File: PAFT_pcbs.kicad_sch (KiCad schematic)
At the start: 15 parts, among them J1 Conn_01x03, J2 Conn_01x03, J4 Screw_Terminal_01x02, J5 Screw_Terminal_01x02, J6 RPi_GPIO, J8 Screw_Terminal_01x02, J9 Screw_Terminal_01x02

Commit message: Updated schematic
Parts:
- removed J4, J5: Screw_Terminal_01x02, TerminalBlock:TerminalBlock_MaiXu_MX126-5.0-02P_1x02_P5.00mm, symbol Connector:Screw_Terminal_01x02
- added J4: Actuator_L, Connector_PinHeader_2.00mm:PinHeader_1x02_P2.00mm_Vertical, symbol Connector_Generic:Conn_01x02
- added J5: Actuator_R, Connector_PinHeader_2.00mm:PinHeader_1x02_P2.00mm_Vertical, symbol Connector_Generic:Conn_01x02
- J1: value Conn_01x03 -> Servo_R; footprint (none) -> Connector_PinHeader_2.00mm:PinHeader_1x03_P2.00mm_Vertical
- J2: value Conn_01x03 -> Servo_L; footprint (none) -> Connector_PinHeader_2.00mm:PinHeader_1x03_P2.00mm_Vertical
- J8: value Screw_Terminal_01x02 -> 12V_In
- J9: value Screw_Terminal_01x02 -> RPi_Terminal
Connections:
- net HBridge/AOUT1: now also J4.1 (Pin_1)
- net HBridge/AOUT2: now also J4.2 (Pin_2)
- net HBridge/BOUT1: now also J5.1 (Pin_1)
- net HBridge/BOUT2: now also J5.2 (Pin_2)
- net HBridge/FAULT_N: now also J6.35 (BCM19_MISO_PCM_FS)
- net HBridge/SLEEP_N: now also J6.37 (BCM26)
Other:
- removed sheet RPiUSBC
- moved on the sheet: J8, J9, TP1, TP2

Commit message: Added footprints
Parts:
- J6: footprint (none) -> RPi_HAT:RPI_Hat_B+
- TP1: value TestPoint -> 12V; footprint (none) -> TestPoint:TestPoint_Plated_Hole_D2.0mm
- TP2: value TestPoint -> GND; footprint (none) -> TestPoint:TestPoint_Plated_Hole_D2.0mm
- TP3: value TestPoint -> 6V; footprint (none) -> TestPoint:TestPoint_Plated_Hole_D2.0mm
- TP4: value TestPoint -> 5V; footprint (none) -> TestPoint:TestPoint_Plated_Hole_D2.0mm
- TP5: value TestPoint -> PWM_R; footprint (none) -> TestPoint:TestPoint_Plated_Hole_D2.0mm
- TP6: value TestPoint -> PWM_L; footprint (none) -> TestPoint:TestPoint_Plated_Hole_D2.0mm
- TP7: value TestPoint -> SDA; footprint (none) -> TestPoint:TestPoint_Plated_Hole_D2.0mm
- TP8: value TestPoint -> SCL; footprint (none) -> TestPoint:TestPoint_Plated_Hole_D2.0mm
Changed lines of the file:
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@@
 			)
 		)
-		(property "Value" "TestPoint"
+		(property "Value" "SDA"
 			(at 106.68 39.8779 0)
 			(effects
@@
 			)
 		)
-		(property "Footprint" ""
+		(property "Footprint" "TestPoint:TestPoint_Plated_Hole_D2.0mm"
 			(at 109.22 41.91 0)
 			(effects
@@
 			)
 		)
-		(property "Value" "TestPoint"
-			(at 29.464 35.052 0)
-			(effects
-				(font
-					(size 1.27 1.27)
-				)
-				(justify left)
-			)
-		)
-		(property "Footprint" ""
+		(property "Value" "5V"
+			(at 35.56 34.29 0)
+			(effects
+				(font
+					(size 1.27 1.27)
+				)
+				(justify left)
+			)
+		)
+		(property "Footprint" "TestPoint:TestPoint_Plated_Hole_D2.0mm"
 			(at 45.72 36.83 0)
 			(effects
@@
 			)
 		)
-		(property "Value" "TestPoint"
+		(property "Value" "PWM_L"
 			(at 149.86 51.5619 0)
 			(effects
@@
 			)
 		)
-		(property "Footprint" ""
+		(property "Footprint" "TestPoint:TestPoint_Plated_Hole_D2.0mm"
 			(at 142.24 46.99 0)
 			(effects
@@
 			)
 		)
-		(property "Value" "TestPoint"
+		(property "Value" "GND"
 			(at 78.74 121.4119 0)
 			(effects
@@
 			)
 		)
-		(property "Footprint" ""
+		(property "Footprint" "TestPoint:TestPoint_Plated_Hole_D2.0mm"
 			(at 71.12 116.84 0)
 			(effects
@@
 			)
 		)
-		(property "Value" "TestPoint"
+		(property "Value" "6V"
 			(at 157.48 24.6379 0)
 			(effects
@@
 			)
 		)
-		(property "Footprint" ""
+		(property "Footprint" "TestPoint:TestPoint_Plated_Hole_D2.0mm"
 			(at 160.02 26.67 0)
 			(effects
@@
 			)
 		)
-		(property "Value" "TestPoint"
+		(property "Value" "PWM_R"
 			(at 149.86 36.0679 0)
 			(effects
@@
 			)
 		)
-		(property "Footprint" ""
+		(property "Footprint" "TestPoint:TestPoint_Plated_Hole_D2.0mm"
 			(at 152.4 38.1 0)
 			(effects
@@
 			)
 		)
-		(property "Value" "TestPoint"
+		(property "Value" "12V"
 			(at 78.74 112.2679 0)
 			(effects
@@
 			)
 		)
-		(property "Footprint" ""
+		(property "Footprint" "TestPoint:TestPoint_Plated_Hole_D2.0mm"
 			(at 81.28 114.3 0)
 			(effects
@@
 			)
 		)
-		(property "Value" "TestPoint"
+		(property "Value" "SCL"
 			(at 106.68 49.0219 0)
 			(effects
@@
 			)
 		)
-		(property "Footprint" ""
+		(property "Footprint" "TestPoint:TestPoint_Plated_Hole_D2.0mm"
 			(at 99.06 44.45 0)
 			(effects
@@
 			)
 		)
-		(property "Footprint" ""
+		(property "Footprint" "RPi_HAT:RPI_Hat_B+"
 			(at 93.98 39.37 0)
 			(effects

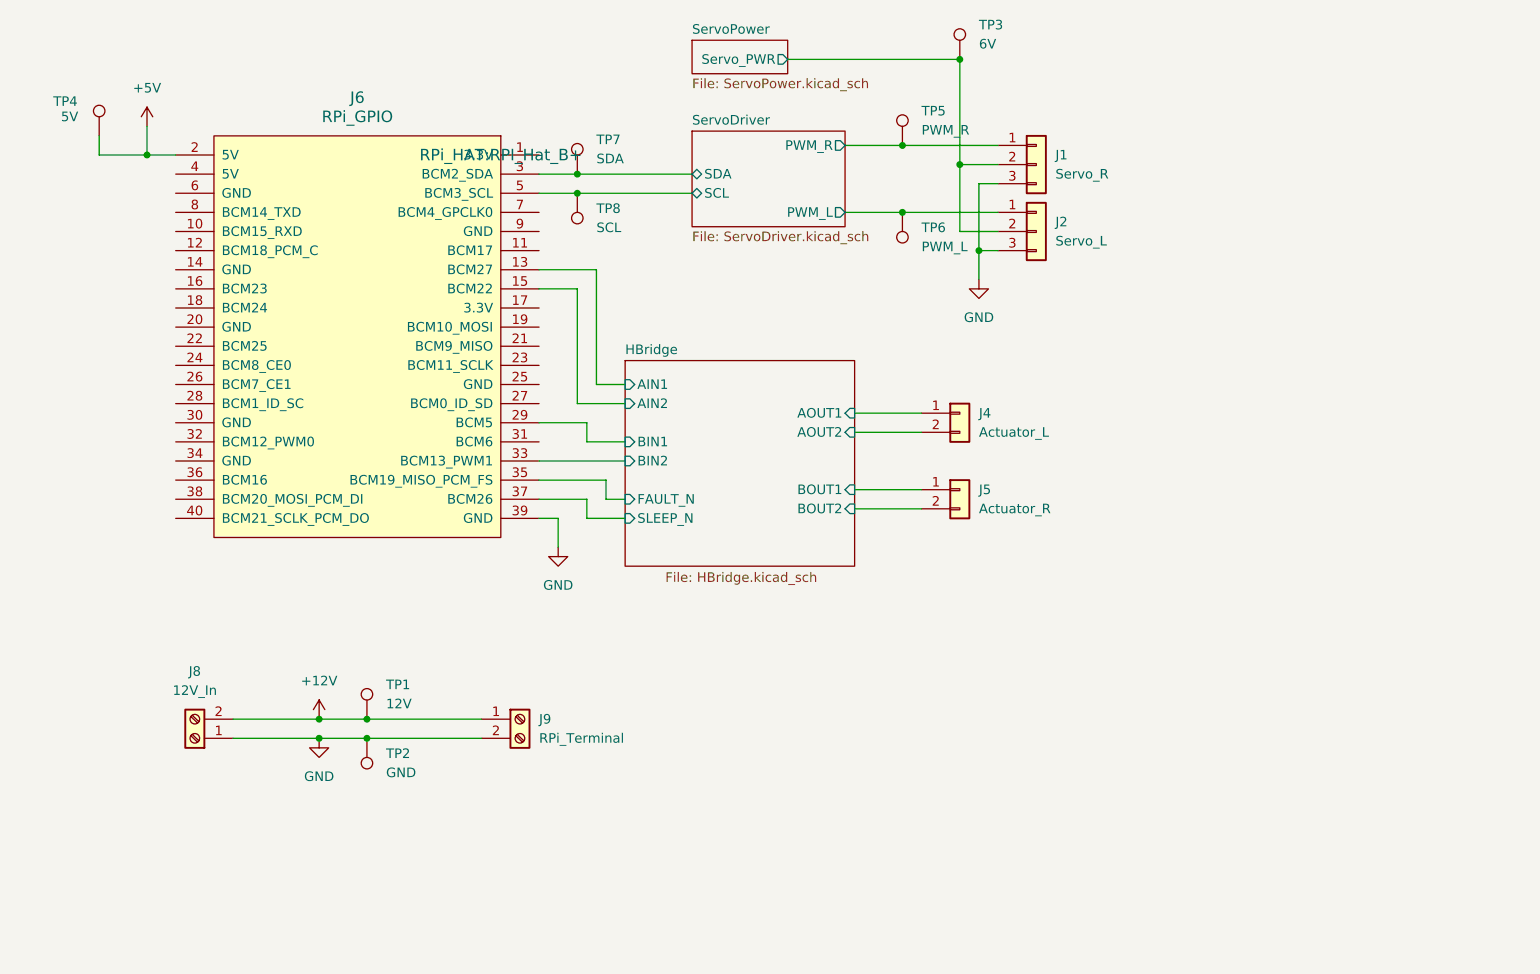
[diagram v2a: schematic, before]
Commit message: PCB Placement and Planes
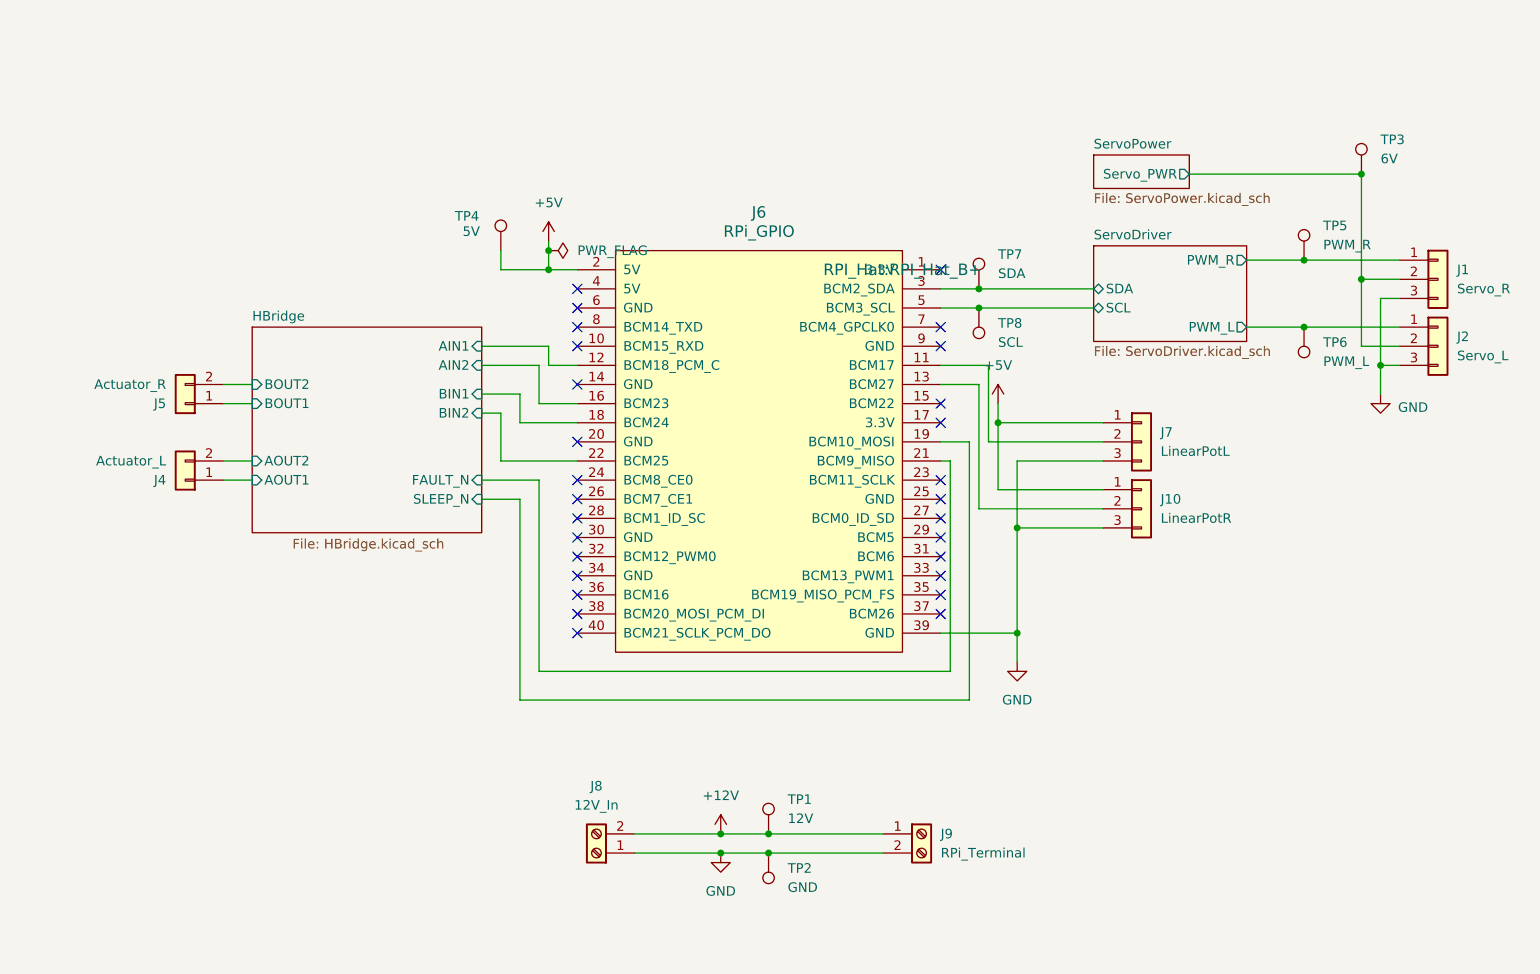
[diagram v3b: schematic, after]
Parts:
- added J10: LinearPotR, Connector_PinHeader_2.00mm:PinHeader_1x03_P2.00mm_Vertical, symbol Connector_Generic:Conn_01x03
- added J7: LinearPotL, Connector_PinHeader_2.00mm:PinHeader_1x03_P2.00mm_Vertical, symbol Connector_Generic:Conn_01x03
- J6: footprint RPi_HAT:RPI_Hat_B+ -> RPI_Hat:RPI_Hat_B+
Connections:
- net +5V: now also J10.1 (Pin_1), J7.1 (Pin_1)
- net GND: now also J10.3 (Pin_3), J7.3 (Pin_3)
- net HBridge/AIN1: now also J6.12 (BCM18_PCM_C); no longer J6.13 (BCM27)
- net HBridge/AIN2: now also J6.16 (BCM23); no longer J6.15 (BCM22)
- net HBridge/BIN1: now also J6.18 (BCM24); no longer J6.29 (BCM5)
- net HBridge/BIN2: now also J6.22 (BCM25); no longer J6.33 (BCM13_PWM1)
- net HBridge/FAULT_N: now also J6.21 (BCM9_MISO); no longer J6.35 (BCM19_MISO_PCM_FS)
- net HBridge/SLEEP_N: now also J6.19 (BCM10_MOSI); no longer J6.37 (BCM26)
- net at J6.11 (BCM17): now also J7.2 (Pin_2)
- new net: J10.2 (Pin_2), J6.13 (BCM27)
- no-connect marks 0 -> 28
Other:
- moved on the sheet: J1, J2, J4, J5, J6, J8, J9, TP1, TP2, TP3, TP4, TP5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

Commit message: Routing adjustments
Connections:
- net +5V: now also J6.4 (5V)
- net GND: now also J6.14 (GND), J6.20 (GND), J6.25 (GND), J6.30 (GND), J6.34 (GND), J6.6 (GND), J6.9 (GND)
- no-connect marks 28 -> 20
